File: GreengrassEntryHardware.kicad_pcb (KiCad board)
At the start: 2 copper layers, 66 x 57 mm, 31 parts, among them J1 USB_B_Micro, J2 GPIOBreakout, J3 Raspberry_Pi_2_3, J4 AutomaticSlidingDoor, J5 MFRC-522, U1 CH340G, Y1 12MHZ

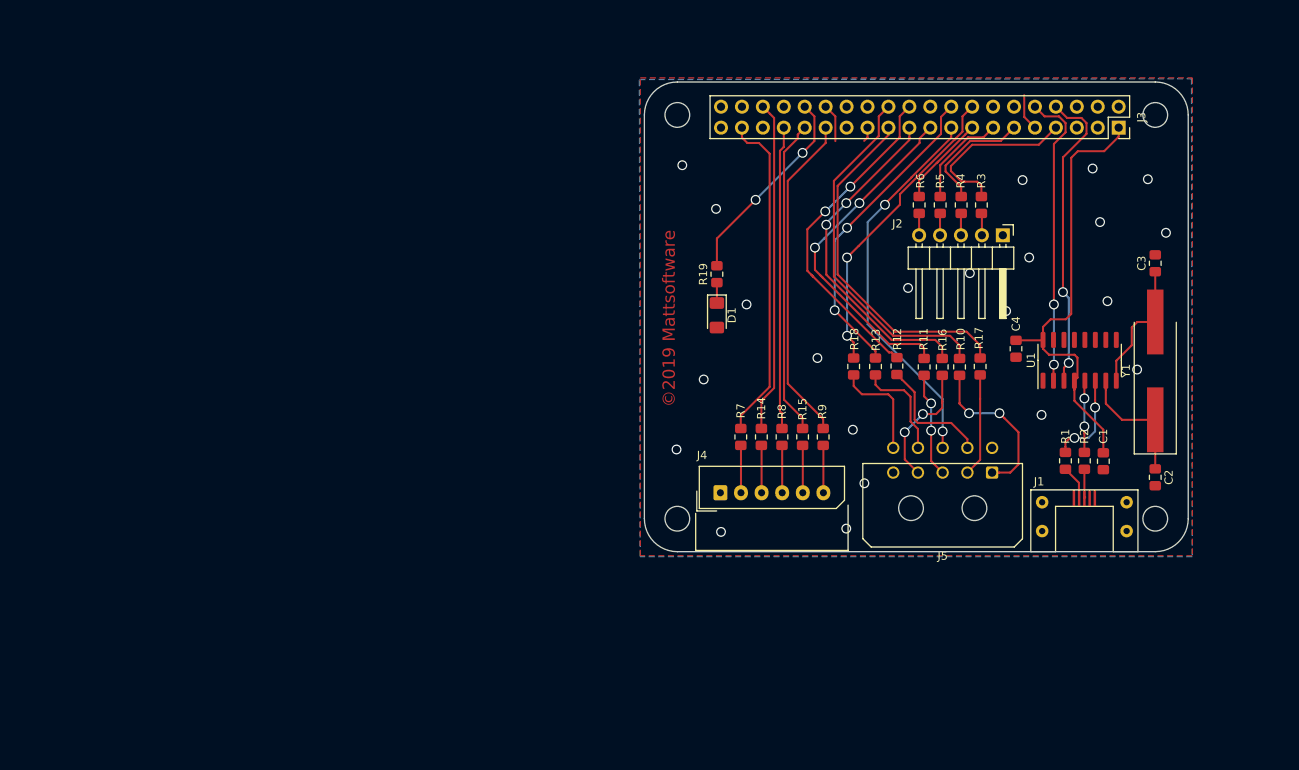
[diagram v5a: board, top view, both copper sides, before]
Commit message: Radical redesign using nets, mini spox, larger board, traces on underside
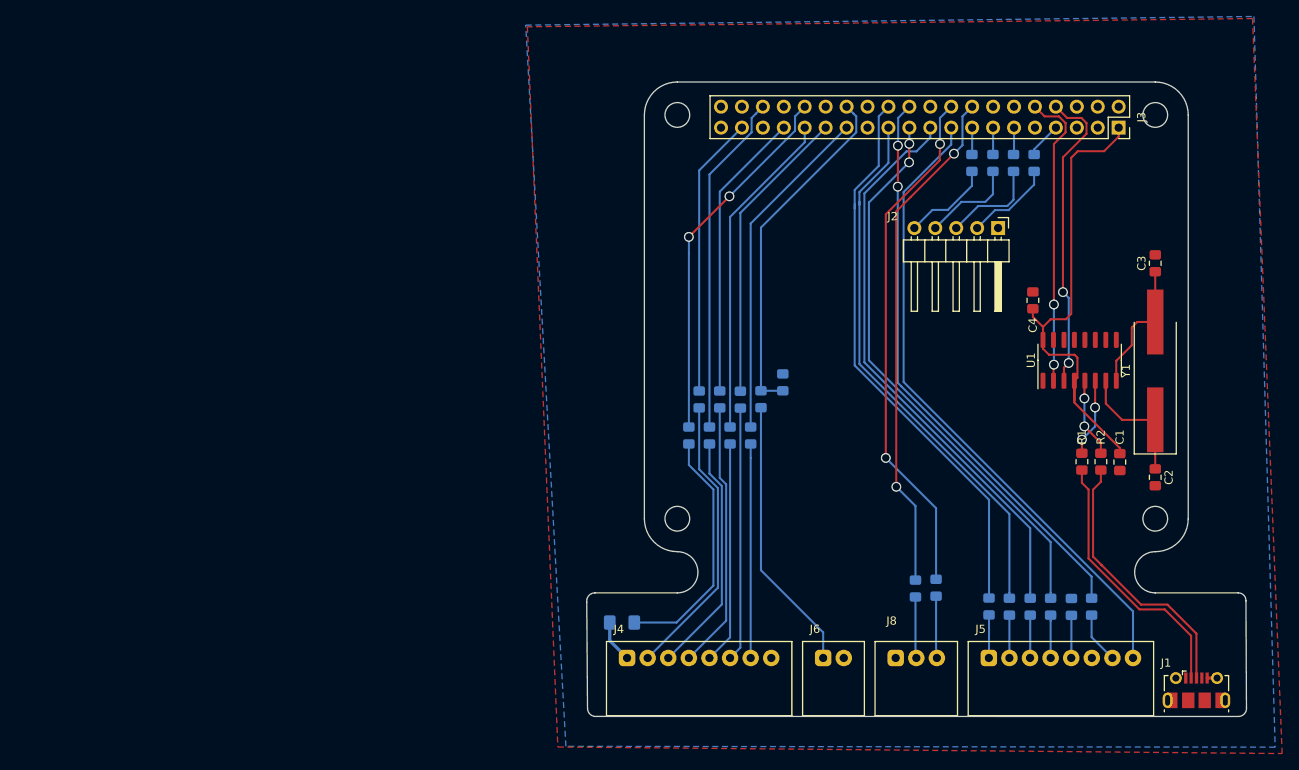
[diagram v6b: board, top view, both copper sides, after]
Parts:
- added J6: DoorEnable, GreengrassEntryHardware:Molex-MiniSpox-22057025-02-Horizontal, F.Cu at (205.7, 120.9)
- added J8: FEEDBACK, GreengrassEntryHardware:Molex-MiniSpox-22057025-03-Horizontal, F.Cu at (214.5, 120.9)
- added R20: 27, Resistor_SMD:R_0805_2012Metric_Pad1.15x1.40mm_HandSolder, B.Cu at (198.2, 89.5)
- added R21: 27, Resistor_SMD:R_0805_2012Metric_Pad1.15x1.40mm_HandSolder, B.Cu at (196.9, 93.9)
- added R22: 10k, Resistor_SMD:R_0805_2012Metric_Pad1.15x1.40mm_HandSolder, B.Cu at (200.8, 87.5)
- added R23: 27, Resistor_SMD:R_0805_2012Metric_Pad1.15x1.40mm_HandSolder, B.Cu at (235.8, 114.7)
- D1, R10, R11, R12, R13, R14, R15, R16, R17, R18, R19, R3, R4, R5, R6, R7, R8, R9: moved to B.Cu
- J1: footprint GreengrassEntryHardware:MicroUSB -> GreengrassEntryHardware:USB_Micro-B_Molex-105017-0001
- J4: footprint GreengrassEntryHardware:Molex_SPOX_5267-06A_1x06_P2.50mm_Horizontal -> GreengrassEntryHardware:Molex-MiniSpox-22057xx5-08-Horizontal
- J5: footprint GreengrassEntryHardware:Molex_Micro-Fit_3.0_43045-1000_2x05_P3.00mm_Horizontal -> GreengrassEntryHardware:Molex-MiniSpox-22057xx5-08-Horizontal
- moved D1 39.0 mm to (181.3, 116.6), turned to 180 degrees
- moved R12 37.6 mm to (238.3, 114.7)
- moved R16 31.9 mm to (233.3, 114.7)
- moved R11 31.8 mm to (230.8, 114.7)
- moved R17 29.4 mm to (228.3, 114.7)
- moved R10 29.3 mm to (225.8, 114.7)
- moved R18 28.7 mm to (219.4, 112.4)
- moved R13 27.4 mm to (216.9, 112.5)
- moved J1 26.1 mm to (251.0, 124.8)
- moved J4 23.0 mm to (181.9, 120.9)
- moved J5 22.5 mm to (225.8, 120.9), turned to 0 degrees
- moved R19 19.9 mm to (189.4, 93.9)
- moved R9 11.0 mm to (195.7, 89.5)
- moved R8 8.82 mm to (193.2, 89.5)
- moved R15 8.80 mm to (194.4, 93.9)
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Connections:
- net /3.3V renamed Net-(J3-Pad17)
- net /AUTO renamed Net-(J4-Pad4)
- net /AUTO_OUT renamed Net-(J4-Pad5)
- net /CLOSED renamed Net-(J4-Pad6)
- net /EXIT renamed Net-(J4-Pad2)
- net /GPIO17 renamed Net-(J2-Pad3)
- net /GPIO22 renamed Net-(J2-Pad5)
- net /GPIO27 renamed Net-(J2-Pad4)
- net /GPIO4 renamed Net-(J2-Pad2)
- net /MISO renamed Net-(J5-Pad4)
- net /MOSI renamed Net-(J5-Pad3)
- net /OPEN renamed Net-(J4-Pad3)
- net /RST renamed Net-(J5-Pad7)
- net /SCK renamed Net-(J5-Pad2)
- net /SDA-CS renamed Net-(J5-Pad1)
- net Net-(J3-Pad11) renamed GPIO17
- net Net-(J3-Pad13) renamed GPIO27
- net Net-(J3-Pad15) renamed GPIO22
- net Net-(J3-Pad19) renamed RFID-MOSI
- net Net-(J3-Pad21) renamed RFID-MISO
- net Net-(J3-Pad22) renamed RFID-RST
- net Net-(J3-Pad23) renamed RFID-SCK
- net Net-(J3-Pad24) renamed RFID-CS
- net Net-(J3-Pad29) renamed AUTO_OUT
- net Net-(J3-Pad31) renamed AUTO
- net Net-(J3-Pad33) renamed OPEN
- net Net-(J3-Pad36) renamed EXIT
- net Net-(J3-Pad37) renamed ACTIVATE
- net Net-(J3-Pad7) renamed GPIO4
- J3 pad 16: Net-(J3-Pad16) -> FEEDBACK-BUZZER
- J3 pad 18: Net-(J3-Pad18) -> FEEDBACK-LED
- J3 pad 27: (no net) -> CLOSED
- J3 pad 28: (no net) -> ENABLE
- J5 pad 5: (no net) -> Net-(J5-Pad5)
- R13 pad 1: /LED -> Net-(J8-Pad2)
- R13 pad 2: Net-(J3-Pad18) -> FEEDBACK-BUZZER
- R18 pad 1: /BUZZER -> Net-(J8-Pad3)
- R18 pad 2: Net-(J3-Pad16) -> FEEDBACK-LED
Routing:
- net FEEDBACK-LED: track 0.00 -> 63.2 mm, vias 0 -> 2
- net FEEDBACK-BUZZER: track 0.00 -> 62.2 mm, vias 0 -> 2
- net ENABLE: track 0.00 -> 42.4 mm
- net CLOSED: track 0.00 -> 41.2 mm
- net Net-(J3-Pad18): track 38.4 -> 0.00 mm, vias 2 -> 0
- net Net-(J3-Pad16): track 37.3 -> 0.00 mm, vias 2 -> 0
- net Net-(J6-Pad1): track 0.00 -> 33.5 mm
- net Net-(J3-Pad17): track 46.8 -> 78.3 mm, vias 2 -> 0
- net RFID-RST: track 40.6 -> 70.0 mm
- net /D+: track 3.69 -> 32.8 mm
- net Net-(J4-Pad2): track 5.76 -> 34.8 mm
- net /D-: track 4.18 -> 32.5 mm
- net Net-(D1-Pad1): track 2.08 -> 29.9 mm
- net RFID-MOSI: track 41.8 -> 69.5 mm, vias 2 -> 0
- net RFID-MISO: track 41.4 -> 68.3 mm
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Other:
- board size 66 x 57 mm -> 80.1 x 77 mm
- net class Power added: clearance 0.2, trace_width 0.4, via_dia 1.2, via_drill 0.9
- board text removed: "©2019 Mattsoftware"

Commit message: Cleanup edge cuts and fill layers, fix some connectors not on back side
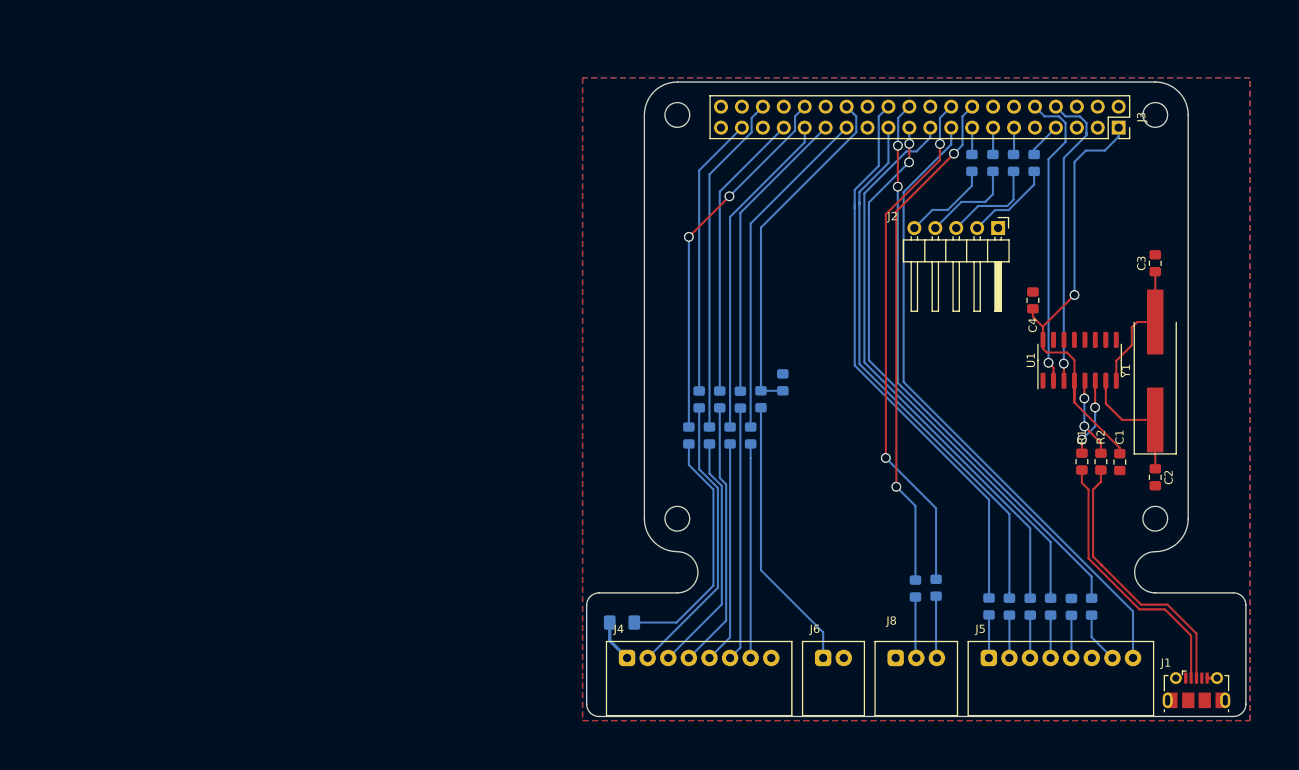
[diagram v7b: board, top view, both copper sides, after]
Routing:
- net Net-(C1-Pad1): track 57.5 -> 55.2 mm, vias 0 -> 1
- net Net-(J3-Pad8): track 37.7 -> 37.1 mm, vias 2 -> 1
- net Net-(J3-Pad10): track 36.5 -> 36.9 mm, vias 2 -> 1
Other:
- board size 80.1 x 77 mm -> 80 x 77 mm

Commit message: Tidy up pcb and annotate with v1.0
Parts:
- moved J1 68.8 mm to (182.3, 128.9)
- moved C4 68.8 mm to (162.4, 81.1)
- moved J2 68.8 mm to (158.2, 72.3)
- moved J5 68.8 mm to (157.1, 124.5)
- moved R12 68.8 mm to (169.6, 118.3)
- moved R13 68.8 mm to (148.2, 116.1)
- moved R16 68.8 mm to (164.6, 118.3)
- moved R17 68.8 mm to (159.6, 118.3)
- moved R18 68.8 mm to (150.7, 116.0)
- moved R2 68.8 mm to (170.7, 100.7)
- moved R20 68.8 mm to (129.4, 93.1)
- moved R21 68.8 mm to (128.2, 97.5)
- moved R22 68.8 mm to (132.1, 91.0)
- moved R3 68.8 mm to (162.6, 64.4)
- moved R4 68.8 mm to (160.1, 64.4)
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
